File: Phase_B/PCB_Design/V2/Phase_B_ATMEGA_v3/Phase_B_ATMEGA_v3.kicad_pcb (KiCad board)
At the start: 2 copper layers, 103.5 x 103.5 mm, 53 parts, among them J1 AVR-ISP-6, J2 USB_B_Mini, J3 ESP_Conn, U1 CA56-12EWA, U2 74HC595, U3 ATmega32U4-A, U4 USBLC6-2SC6, U5 LP2985-3.3, Y1 16MHz

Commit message: Placement Tinkering
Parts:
- moved J1 50.4 mm to (94.5, 130.5)
- moved R16 41.7 mm to (67.5, 118.0)
- moved R13 41.1 mm to (100.8, 146.5), turned to -90 degrees
- moved R5 39.4 mm to (107.9, 105.5)
- moved R10 37.8 mm to (114.5, 105.5)
- moved R6 33.1 mm to (102.1, 105.5)
- moved U5 32.2 mm to (149.8, 147.2)
- moved F1 24.1 mm to (72.3, 155.2)
- moved C3 23.3 mm to (89.0, 162.2)
- moved Y1 23.3 mm to (83.8, 157.7)
- moved C2 23.3 mm to (89.0, 159.7)
- moved C1 22.8 mm to (136.5, 131.7)
- moved C8 20.4 mm to (93.5, 151.5)
- moved R15 18.9 mm to (72.3, 142.2)
- moved C10 17.9 mm to (93.5, 147.0)
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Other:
- board size 103.5 x 103.5 mm -> 102 x 102 mm

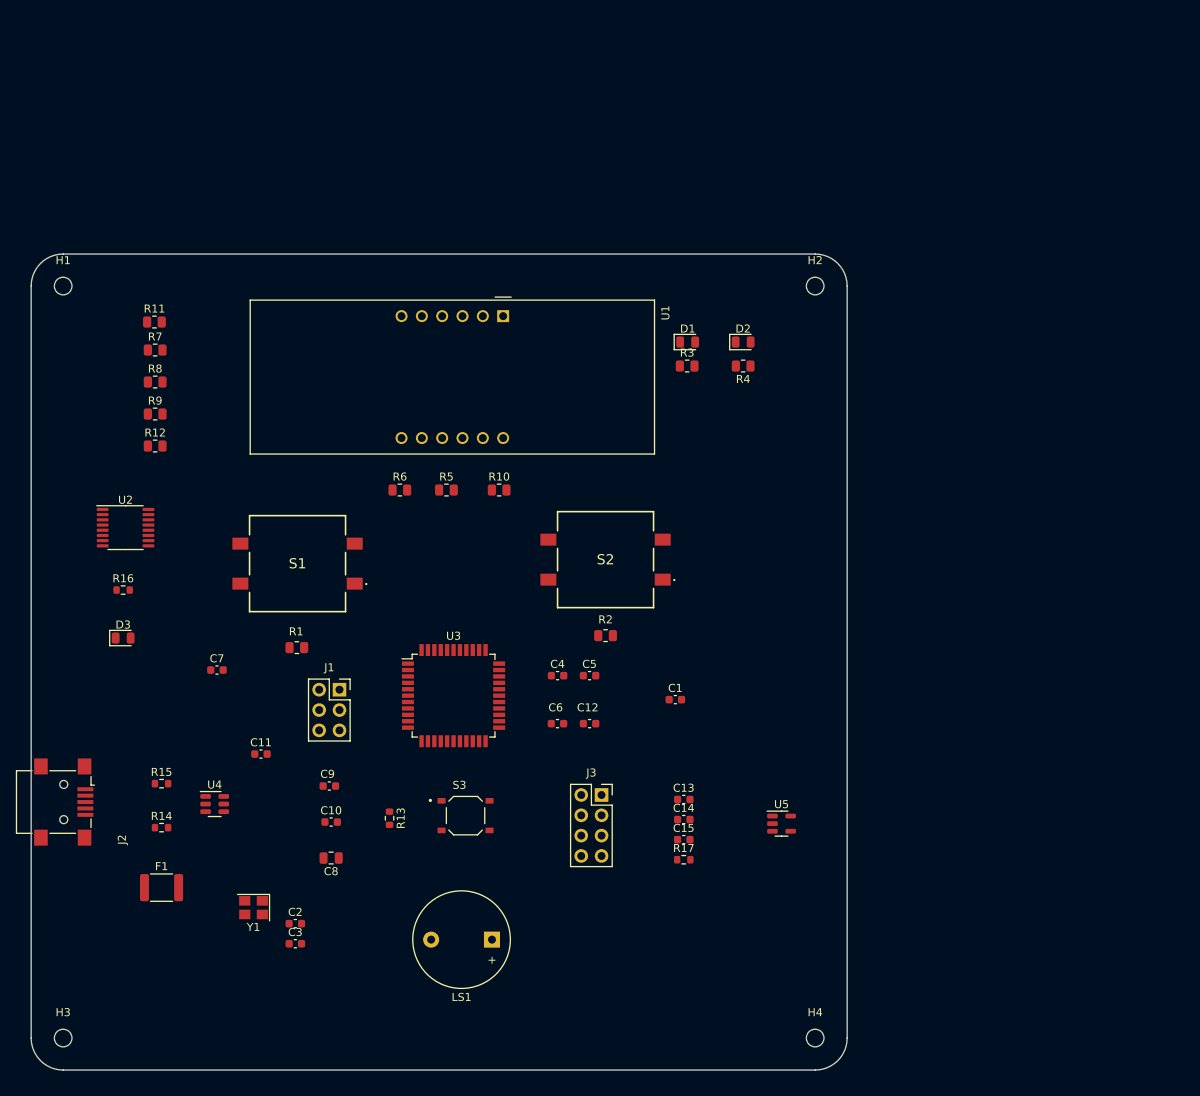
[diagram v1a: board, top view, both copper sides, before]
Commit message: Added housing files and add missing 3d models in PCB viewer for V2
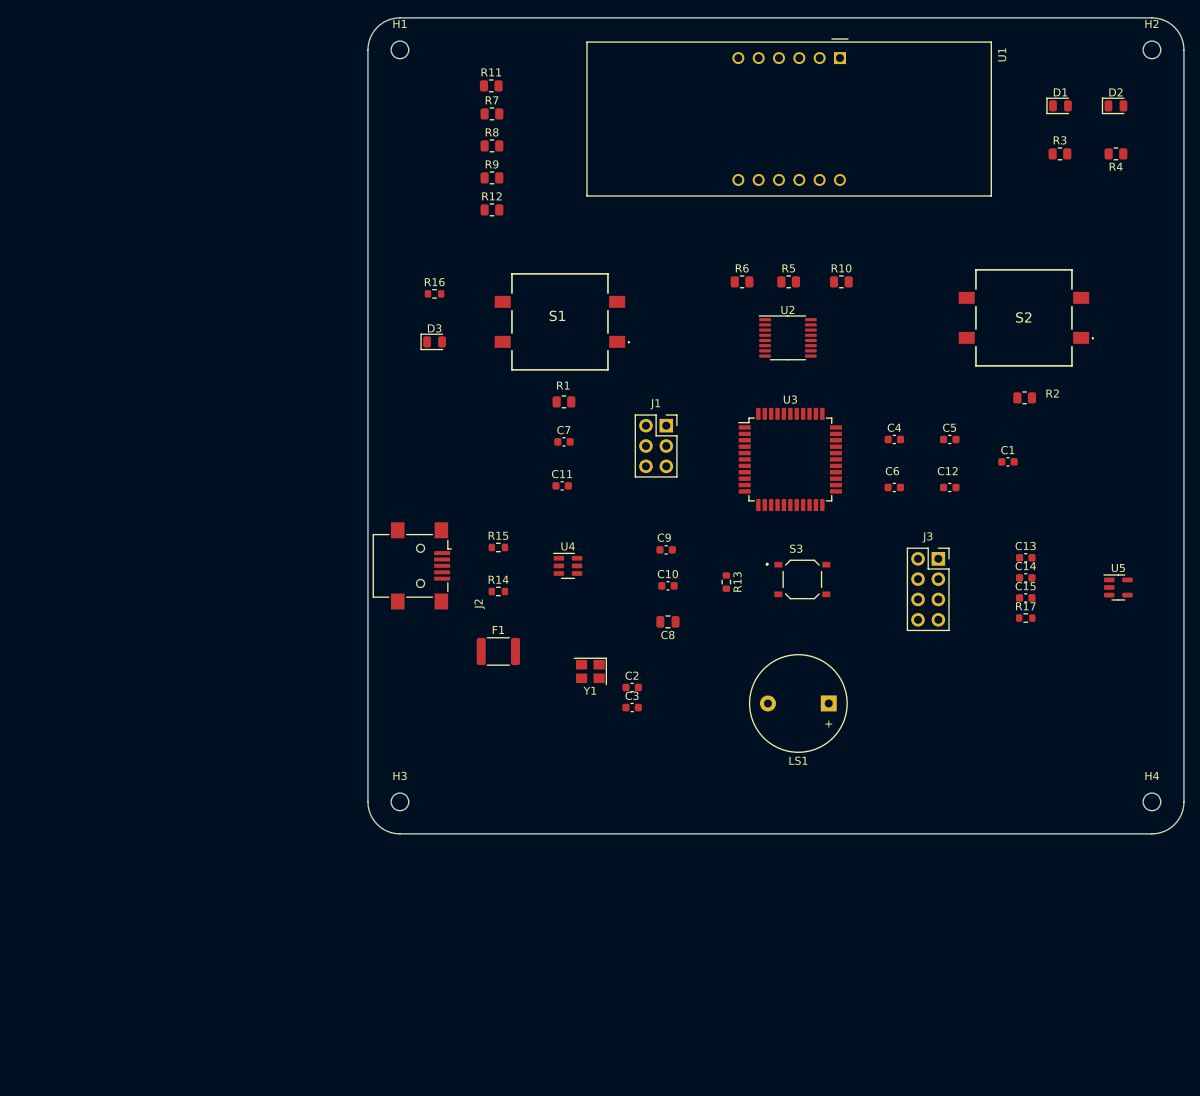
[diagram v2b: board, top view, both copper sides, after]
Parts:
- moved U2 86.1 mm to (150.6, 86.5)
- moved S2 60.4 mm to (180.1, 84.0)
- moved R2 60.2 mm to (180.2, 94.0)
- moved D1 55.2 mm to (184.7, 57.5)
- moved D2 55.2 mm to (191.6, 57.5)
- moved C12 53.8 mm to (170.8, 105.2)
- moved C5 53.8 mm to (170.8, 99.2)
- moved D3 53.7 mm to (106.4, 87.0)
- moved R16 53.7 mm to (106.4, 81.0)
- moved R3 53.6 mm to (184.6, 63.5)
- moved R4 53.6 mm to (191.6, 63.5)
- moved J2 53.5 mm to (104.7, 115.0)
- moved U4 53.3 mm to (123.1, 115.0)
- moved U1 53.0 mm to (157.1, 51.5)
- moved J1 52.5 mm to (135.4, 97.5)
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
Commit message: Routing for V2
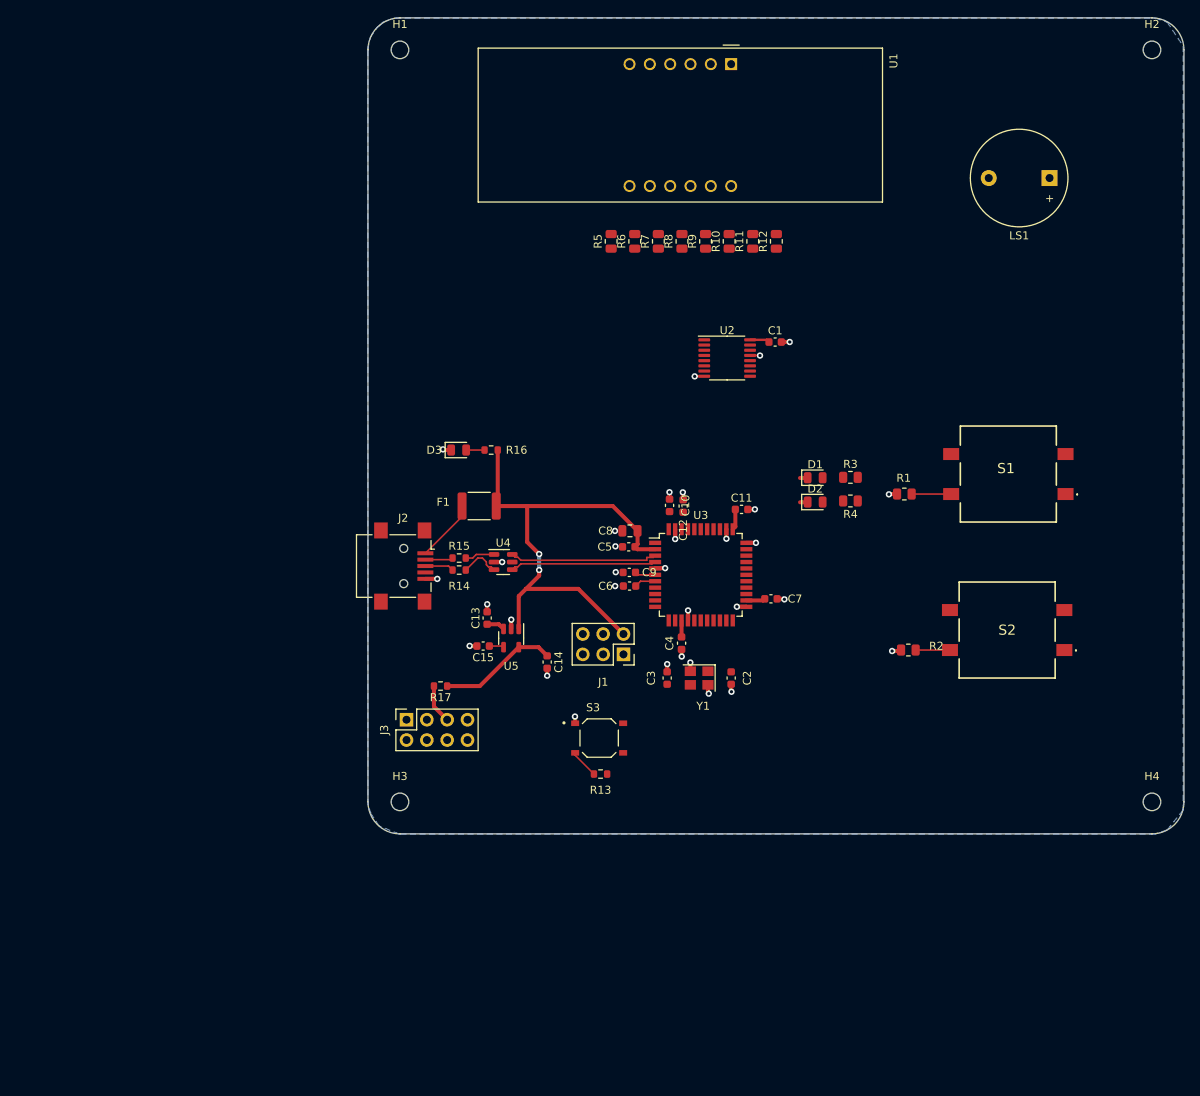
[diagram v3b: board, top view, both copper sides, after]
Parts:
- moved U5 76.2 mm to (116.0, 124.0), turned to -90 degrees
- moved R17 73.6 mm to (107.2, 130.0), turned to 180 degrees
- moved LS1 71.2 mm to (183.3, 66.5)
- moved J3 69.5 mm to (102.9, 134.2), turned to 90 degrees
- moved C15 68.1 mm to (112.5, 125.0), turned to 180 degrees
- moved C13 67.7 mm to (113.0, 121.5), turned to 90 degrees
- moved D2 62.2 mm to (154.0, 107.0)
- moved C14 60.7 mm to (120.5, 127.0), turned to -90 degrees
- moved S1 59.2 mm to (178.2, 103.5)
- moved D1 55.7 mm to (154.0, 104.0)
- moved R4 54.6 mm to (158.4, 106.9)
- moved R3 48.2 mm to (158.4, 103.9)
- moved R1 44.1 mm to (165.2, 106.0)
- moved C5 42.3 mm to (130.7, 112.6), turned to 180 degrees
- moved S2 39.1 mm to (178.0, 123.0)
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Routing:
- net +5V: track 0.00 -> 76.9 mm, vias 0 -> 2
- net GND: track 0.00 -> 32.0 mm, vias 0 -> 32
- net USB_D-: track 0.00 -> 18.6 mm
- net USB_D+: track 0.00 -> 18.3 mm
- net +3.3V: track 0.00 -> 15.0 mm
- net Net-(J2-VBUS): track 0.00 -> 7.80 mm
- net USB_CONN_D+: track 0.00 -> 4.96 mm
- net Button_1: track 0.00 -> 4.94 mm
- net Net-(J3-Pin_5): track 0.00 -> 4.89 mm
- net Button_2: track 0.00 -> 4.29 mm
- net USB_CONN_D-: track 0.00 -> 3.72 mm
- net RST: track 0.00 -> 3.62 mm
- net Net-(J2-D+): track 0.00 -> 3.61 mm
- net Net-(J2-D-): track 0.00 -> 3.48 mm
- net /UCAP: track 0.00 -> 2.58 mm
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- added copper zone on B.Cu, net GND

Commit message: Phase B Update: Routing, BOM Files, Drill Files, Gerber Files, and Assembly PDF
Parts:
- added H5: MountingHole, MountingHole:MountingHole_2.2mm_M2, F.Cu at (153.9, 102.4)
- moved R11 44.8 mm to (104.5, 58.0)
- moved R12 44.6 mm to (105.0, 68.2)
- moved R9 35.7 mm to (105.5, 82.2)
- moved R8 32.4 mm to (105.0, 74.9)
- moved R7 31.5 mm to (105.0, 63.0)
- moved R3 21.6 mm to (160.5, 82.5), turned to 180 degrees
- moved D1 21.6 mm to (156.1, 82.5)
- moved D2 21.6 mm to (156.1, 85.5)
- moved R4 21.6 mm to (160.5, 85.4)
- moved R6 21.6 mm to (150.5, 84.5)
- moved C1 18.0 mm to (131.0, 87.5), turned to 180 degrees
- moved R5 17.8 mm to (146.2, 76.4)
- moved U2 6.95 mm to (137.0, 85.5), turned to 180 degrees
- moved R10 3.28 mm to (140.0, 74.0)
- moved U1 2.29 mm to (143.8, 54.5)
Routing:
- net +5V: track 76.9 -> 271.5 mm, vias 2 -> 11
- net Dig2: track 0.00 -> 180.6 mm, vias 0 -> 6
- net Dig4: track 0.00 -> 154.6 mm, vias 0 -> 6
- net ST_CP: track 0.00 -> 142.8 mm, vias 0 -> 8
- net DS: track 0.00 -> 142.5 mm, vias 0 -> 8
- net Dig3: track 0.00 -> 132.5 mm, vias 0 -> 4
- net GREEN_LED: track 0.00 -> 122.2 mm, vias 0 -> 4
- net dp: track 0.00 -> 120.9 mm
- net Buzzer: track 0.00 -> 112.8 mm, vias 0 -> 4
- net g: track 0.00 -> 108.2 mm, vias 0 -> 2
- net Dig1: track 0.00 -> 92.1 mm, vias 0 -> 8
- net RED_LED: track 0.00 -> 87.2 mm, vias 0 -> 6
- net c: track 0.00 -> 82.8 mm, vias 0 -> 2
- net RX: track 0.00 -> 76.8 mm, vias 0 -> 8
- net TX: track 0.00 -> 75.6 mm, vias 0 -> 4
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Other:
- board text added: "Leonel Gomez Embedded Systems Kitchen Timer v2.0 04-20-2023"

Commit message: Gerber File Update, Adjusted Board Dimension, etc.
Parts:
- removed H3: MountingHole, MountingHole:MountingHole_2.2mm_M2
- added H4: MountingHole, MountingHole:MountingHole_2.2mm_M2, F.Cu at (103.1, 125.9)
- moved H2 11.8 mm to (189.2, 60.0)
- moved H4 9.00 mm to (191.4, 136.8)
- moved H1 2.56 mm to (104.0, 52.2)
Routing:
- net DS: track 142.5 -> 132.4 mm
- net ST_CP: track 142.8 -> 134.5 mm
- net Buzzer: track 112.8 -> 104.8 mm
- net Dig2: track 180.6 -> 174.1 mm
- net GREEN_LED: track 122.2 -> 116.3 mm
- net Dig4: track 154.6 -> 151.4 mm
- net c: track 82.8 -> 79.6 mm
- net RX: track 76.8 -> 74.3 mm
- net TX: track 75.6 -> 73.2 mm
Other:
- board size 102 x 102 mm -> 100 x 100 mm
